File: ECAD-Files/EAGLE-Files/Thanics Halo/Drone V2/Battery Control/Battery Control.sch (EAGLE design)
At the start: 31 parts, among them J1 JST-XH_5POS, J2 SPRING_BTB_8POS_FEMALE, J3 JST_SH_6POS_SIDE, U1 MCP9700-E/TO, U2 2N7002P_MOSFET, U3 DMP3030SN_MOSFET, U4 TS30012, U5 ATTINY20-SSU14S1-M, U6 ATTINY44A-SSU14S1-M

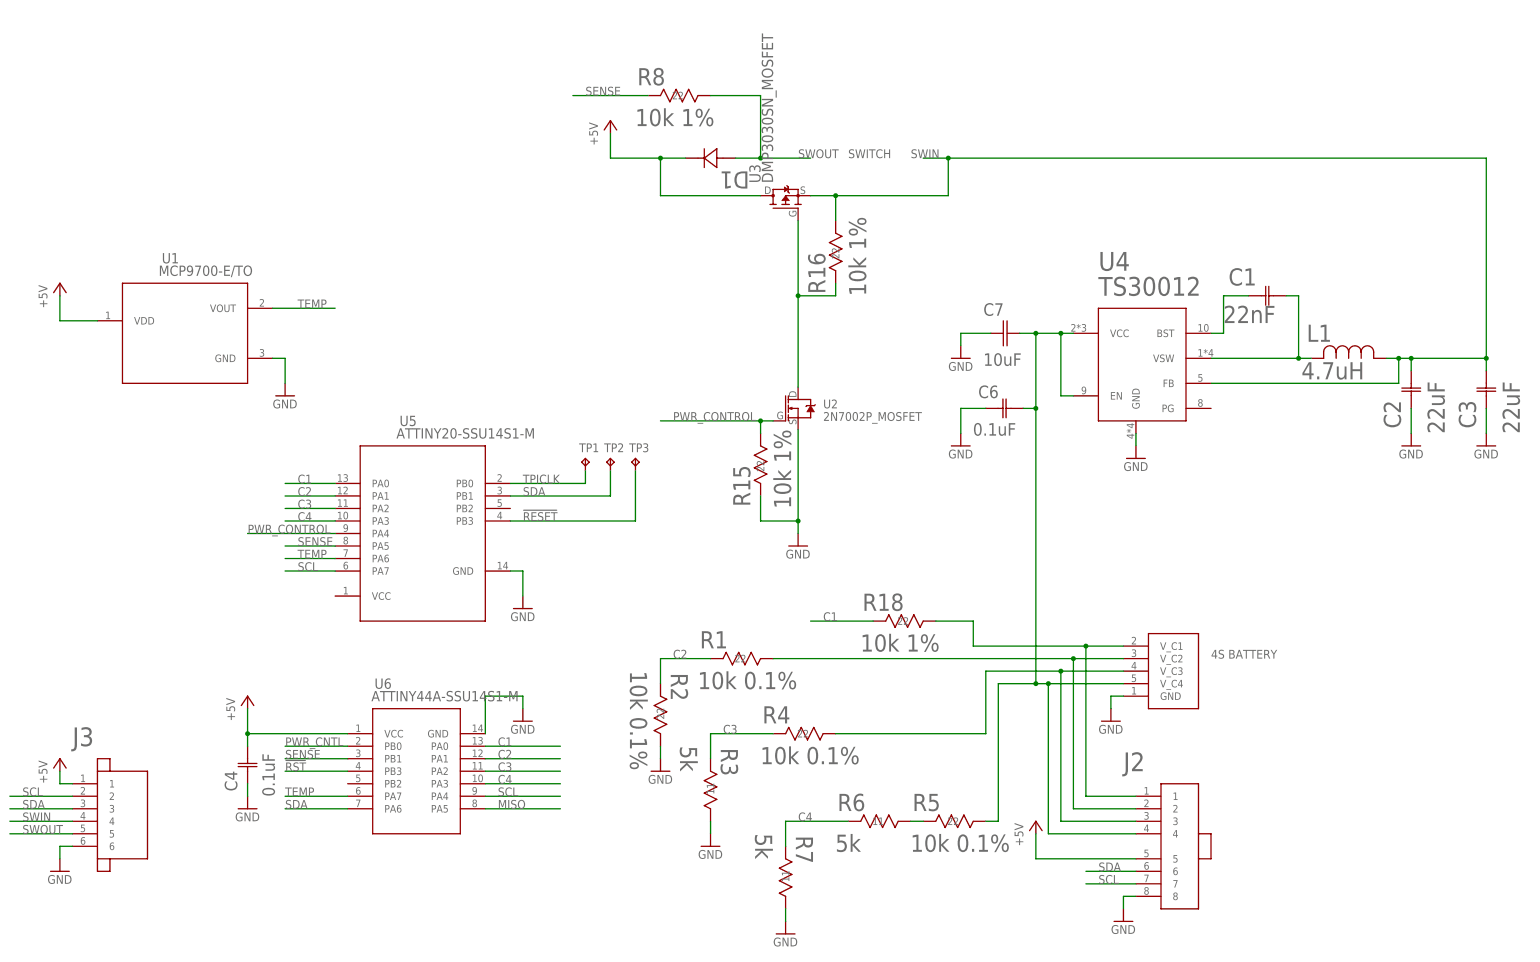
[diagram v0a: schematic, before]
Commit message: Added new battery and joystick modules
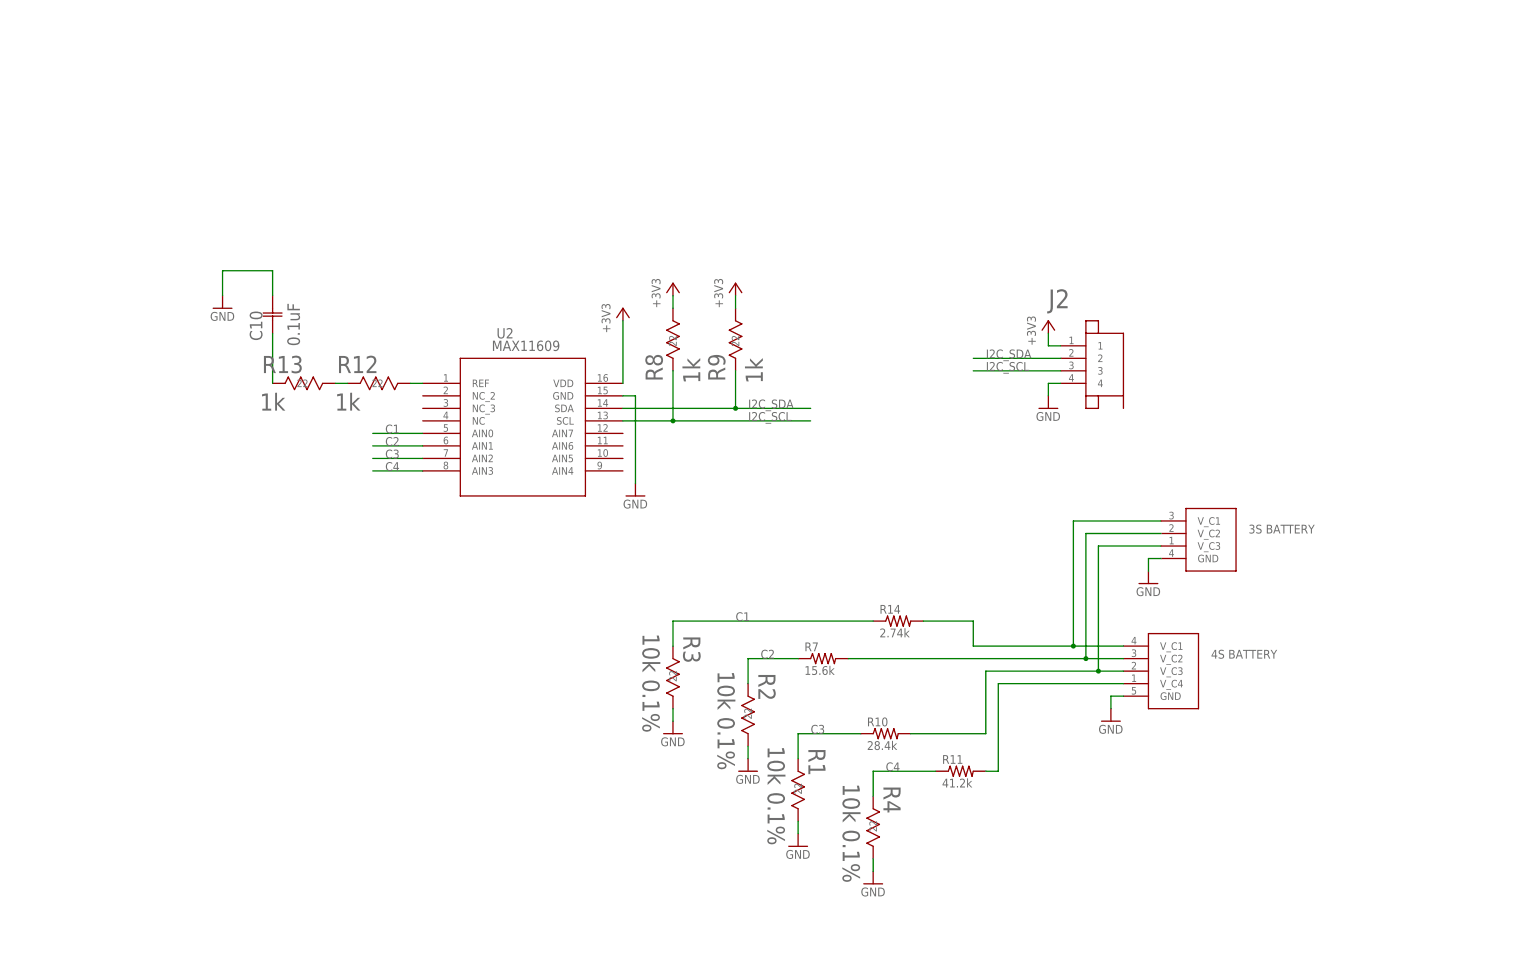
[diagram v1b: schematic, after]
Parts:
- removed C1: 22nF, 22nF-capacitor:GRM155R71H223KA12DG-155-M
- removed C2, C3: 22uF, 22uF X5R Ceramic Capacitor:GRM21BR60J226ME39L
- removed C4, C6: 0.1uF, 0.1uF X7R Ceramic Capacitor:08055C104KAT2A
- removed C7: 10uF, thanics_robotics:10UF_CAPACITOR
- removed D1: (no value), 1n4148w-diode:1N4148W-7-FSOD123-M
- removed L1: 4.7uH, 4.7uH-inductor:DFE252012P-4R7M=P2"
- removed R15, R16, R18: 10k 1%, 10k-resistor:ERA-6AEB103V
- removed R5: 10k 0.1%, 10k-resistor:ERA-6AEB103V
- removed R6: 5k, 5k-resistor:PNM0402E5001BST1
- removed TP1, TP2, TP3: TPB2,54, testpad:TPB2,54
- removed U1: MCP9700-E/TO, mcp9700-temp:MCP9700-E/TO
- removed U3: DMP3030SN_MOSFET, thanics_robotics:DMP3030SN_MOSFET
- removed U4: TS30012, thanics_robotics:TS30012
- removed U5: ATTINY20-SSU14S1-M, attiny20:ATTINY20-SSU14S1-M
- removed U6: ATTINY44A-SSU14S1-M, attiny44:ATTINY44A-SSU14S1-M
- added C10: 0.1uF, Controller Board:08055C104KAT2A
- added R10: 28.4k, thanics-resistor:RT0603BRD0728K4L
- added R11: 41.2k, thanics-resistor:ERA-3AEB4122V
- added R12, R13, R9: 1k, Controller Board:RC0603JR-071KLRC0603N-M
- added R14: 2.74k, thanics-resistor:ERA-3AEB2741V
- J1: value JST-XH_5POS -> JST-XH_4POS; device thanics_robotics:JST-XH_5POS -> thanics-connector:JST-XH_4POS
- J2: value SPRING_BTB_8POS_FEMALE -> (none); device thanics_robotics:SPRING_BTB_8POS_FEMALE -> thanics_robotics:JST_SH_4POS
- J3: value JST_SH_6POS_SIDE -> JST-XH_5POS; device thanics_robotics:JST_SH_6POS_SIDE -> thanics-connector:JST-XH_5POS
- R3: value 5k -> 10k 0.1%; device 5k-resistor:PNM0402E5001BST1 -> 10k-resistor:ERA-6AEB103V
- R7: value 5k -> 15.6k; device 5k-resistor:PNM0402E5001BST1 -> thanics-resistor:TNPW040215K6BEED
- R8: value 10k 1% -> 1k; device 10k-resistor:ERA-6AEB103V -> Controller Board:RC0603JR-071KLRC0603N-M
- U2: value 2N7002P_MOSFET -> MAX11608EEE+21-0055H_16-M; device thanics_robotics:2N7002P_MOSFET -> 8ch ADC:MAX11608EEE+21-0055H_16-M
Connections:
- removed net !RESET: TP3.TP, U5.PB3
- removed net !RST: U6.PB3
- removed net +5V: C4.2, D1.12, J2.5, J3.1, U1.VDD, U3.D, U6.VCC
- removed net MISO: U6.PA5
- removed net N$14: R5.22, R6.22
- removed net N$2: C1.11, U4.BST
- removed net N$3: C1.22, L1.2, U4.VSW
- removed net PWR_CNTL: U6.PB0
- removed net PWR_CONTROL: R15.11, U2.G, U5.PA4
- removed net SCL: J2.7, J3.2, U5.PA7, U6.PA4
- removed net SDA: J2.6, J3.3, TP2.TP, U5.PB1, U6.PA6
- removed net SENSE: R8.22, U5.PA5, U6.PB1
- removed net SWIN: C2.22, C3.22, J3.4, L1.1, R16.11, U3.S, U4.FB
- removed net SWOUT: D1.21, J3.5, R8.11
- removed net TEMP: U1.VOUT, U5.PA6, U6.PA7
- removed net TPICLK: TP1.TP, U5.PB0
- new net +3V3: J2.1, R8.11, R9.11, U2.VDD
- new net I2C_SCL: J2.3, R8.22, U2.SCL
- new net I2C_SDA: J2.2, R9.22, U2.SDA
- new net N$24: R12.22, R13.11
- new net N$28: C10.1, R13.22
- net C1: now also R14.1, R3.22, U2.AIN0; no longer R18.22, U5.PA0, U6.PA0
- net C2: now also R7.1, U2.AIN1; no longer R1.22, U5.PA1, U6.PA1
- net C3: now also R1.22, R10.1, U2.AIN2; no longer R3.11, R4.22, U5.PA2, U6.PA2
- net C4: now also R11.1, R4.22, U2.AIN3; no longer R6.11, R7.11, U5.PA3, U6.PA3
- net GND: now also C10.2, J2.4, J3.GND, R1.11, R3.11, R4.11, U2.GND; no longer C2.11, C3.11, C4.1, C6.1, C7.1, J2.8, J3.6, R15.22, R3.22, R7.22, U1.GND, U2.S, U4.GND, U5.GND, U6.GND
- net N$1: now also R12.11, U2.REF; no longer R16.22, U2.D, U3.G
- net N$10: now also J3.V_C2, R7.2; no longer J2.2, R1.11
- net N$13: now also J3.V_C3, R10.2; no longer J2.3, R4.11
- net N$16: now also J3.V_C4, R11.2; no longer C6.2, C7.2, J1.V_C4, J2.4, R5.11, U4.EN, U4.VCC
- net N$8: now also J3.V_C1, R14.2; no longer J2.1, R18.11
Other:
- note removed: "SWITCH"
- moved on the sheet: R1, R2, R3, R4, R8
